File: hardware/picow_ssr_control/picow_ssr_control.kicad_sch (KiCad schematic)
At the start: 25 parts, among them Q1 IRF4905, U1 RaspberryPi-PicoW, U2 ULN2803A

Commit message: Added Copyright and logos etc.
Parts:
- S1: Mouser Part Number 774-1938MS -> (none)
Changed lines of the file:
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@@
   (title_block
     (title "Picow SSR Control")
-    (date "2022-07-23")
-    (rev "0.0.1")
+    (date "2022-07-26")
+    (rev "0.0.3")
     (comment 2 "http://creativecommons.org/licenses/by-sa/4.0/")
     (comment 3 "License: CC By SA 4.0")
@@
       (effects (font (size 1.27 1.27)) hide)
     )
-    (property "Mouser Part Number" "774-1938MS" (id 6) (at 238.76 135.89 0)
+    (property "Mouser Price/Stock" "https://www.mouser.com/ProductDetail/CTS-Electronic-Components/193-8MS?qs=Mr%252BgrRYddfpU71WCaMSCKA%3D%3D" (id 11) (at 241.3 135.89 0)
       (effects (font (size 1.27 1.27)) (justify left) hide)
     )
-    (property "Mouser Price/Stock" "https://www.mouser.com/ProductDetail/CTS-Electronic-Components/193-8MS?qs=Mr%252BgrRYddfpU71WCaMSCKA%3D%3D" (id 7) (at 241.3 135.89 0)
-      (effects (font (size 1.27 1.27)) (justify left) hide)
-    )

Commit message: Added Updated symbol, footprint, 3d model for zener diode
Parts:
- ZD1: footprint Diode_SMD:D_SMF -> Picow_control:BZD27C10P-M3-08; symbol Device:D_Zener_Small_Filled -> Picow_control:BZD27C10P-M3-08; Characteristics (none) -> 10V 800mW; Height (mm) (none) -> 1.08; MFN (none) -> Vishay Semiconductors; MFP (none) -> BZD27C10P-M3-08; Mfr Vishay Semiconductors -> (none); Mfr # BZD27C10P-M3-08 -> (none); Mouser # 78-BZD27C10P-M3-08 -> (none); Mouser Part Number (none) -> 78-BZD27C10P-M3-08; Mouser Price/Stock (none) -> https://www.mouser.com/ProductDetail/Vishay-Semiconductors/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; Package (none) -> SMF (DO-219AB); Type (none) -> SMD

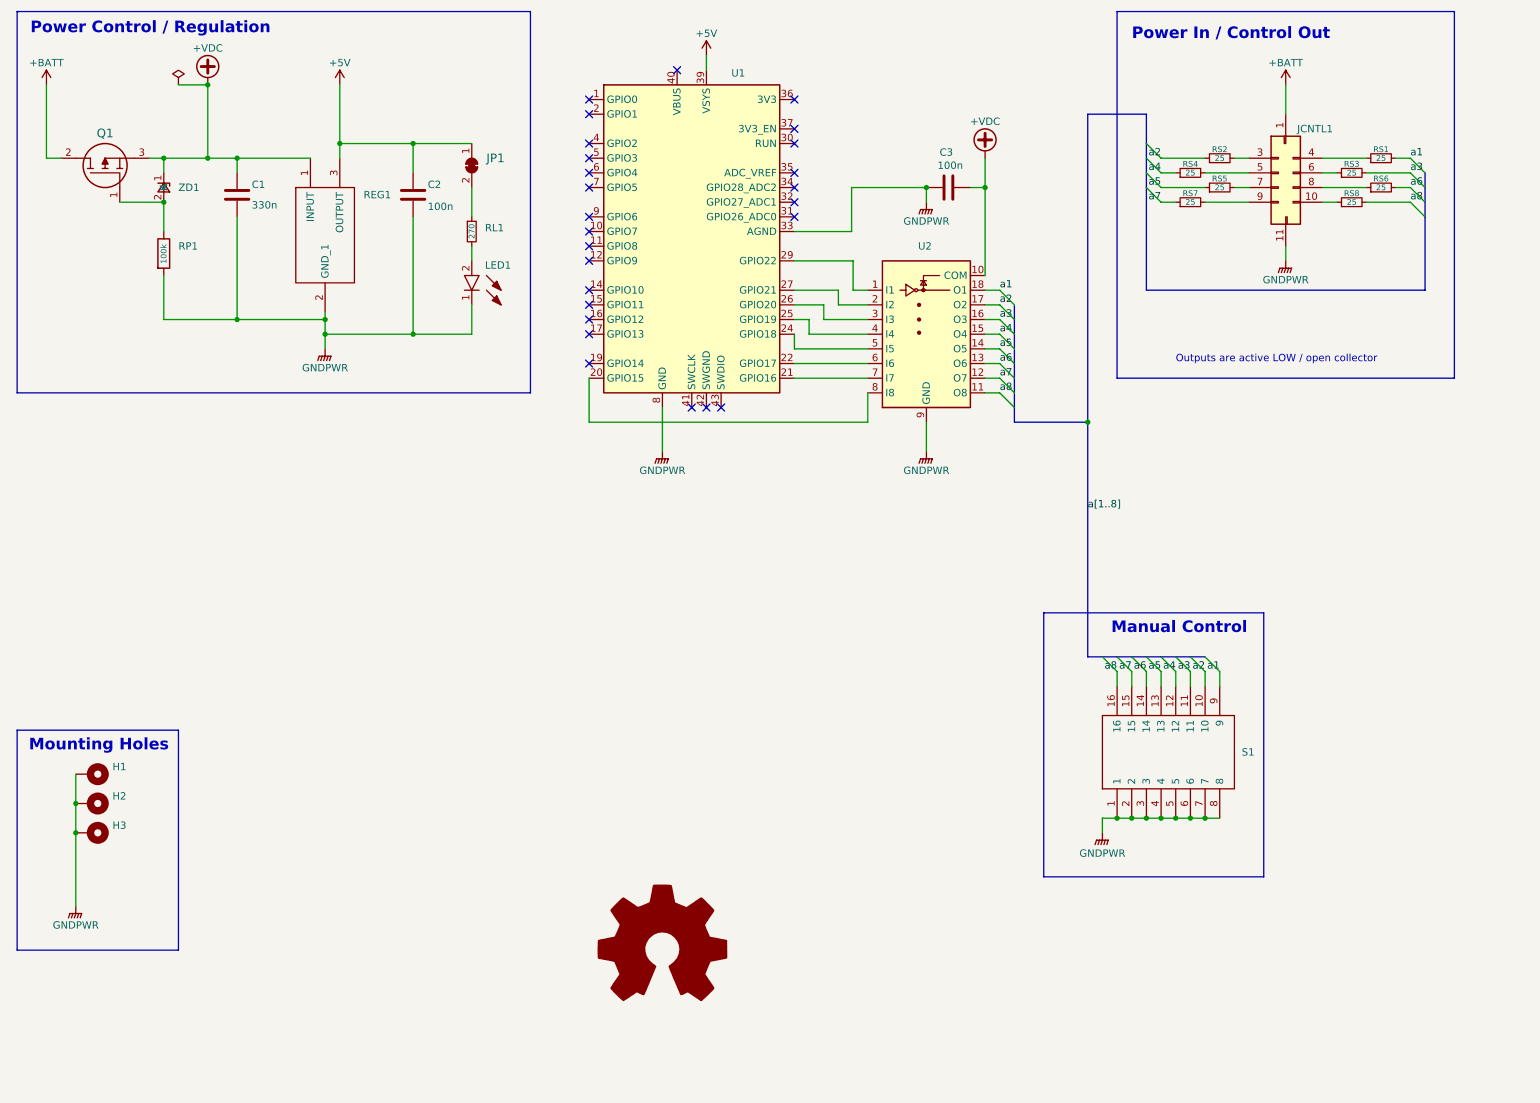
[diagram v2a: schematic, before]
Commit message: Add new Cern licensing info
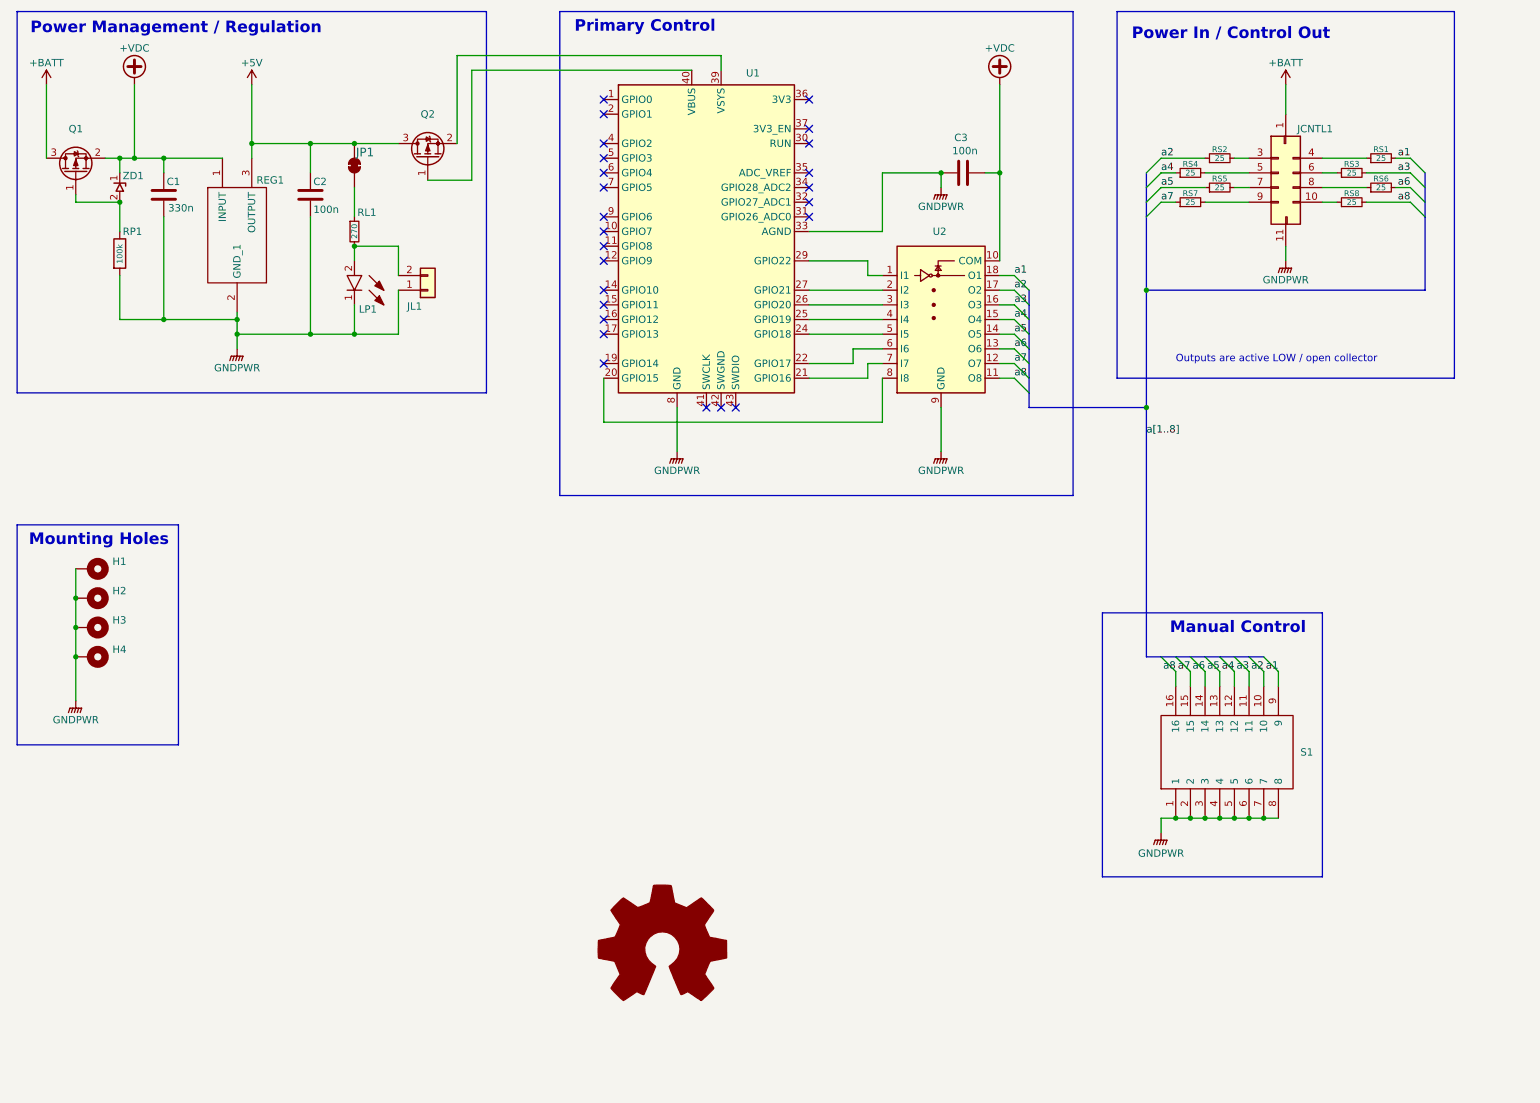
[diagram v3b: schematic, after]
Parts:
- removed Q1: IRF4905, dragon_mobile:TO254P469X1042X1967-3P, symbol dragon_mobile:IRF4905PBF
- added H4: MountingHole_Pad, MountingHole:MountingHole_3.2mm_M3_Pad_Via, symbol Mechanical:MountingHole_Pad
- added JL1: Conn_01x02, Connector_PinHeader_1.00mm:PinHeader_1x02_P1.00mm_Vertical, symbol Connector_Generic:Conn_01x02
- added Q1, Q2: DMG2301L, Package_TO_SOT_SMD:SOT-23, symbol Picow_control:DMG2301L
- RL1: Characteristics (none) -> 270Ohms; 300mW; SMD (0603) 5% Anti Surge AEC-Q200; MFN (none) -> ROHM Semiconductor; MFP (none) -> SDR03EZPJ271; Mfr. #: SDR03EZPJ271 -> (none); Mfr.: ROHM Semiconductor -> (none); Mouser #: 755-SDR03EZPJ271 -> (none); Mouser Part Number (none) -> 755-SDR03EZPJ271; Mouser Price/Stock (none) -> https://www.mouser.com/ProductDetail/ROHM-Semiconductor/SDR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; Package (none) -> 0603; Type (none) -> SMD
- RP1: Characteristics (none) -> 100Kohm 300mW 1% Anti Surge AEC-Q200; Height (mm) (none) -> 0.45; MFN (none) -> ROHM Semiconductor; MFP (none) -> SDR03EZPF1003; Mfr. #: SDR03EZPF1003 -> (none); Mfr.: ROHM Semiconductor -> (none); Mouser Part Number (none) -> 755-SDR03EZPF1003; Mouser Price/Stock (none) -> https://www.mouser.com/ProductDetail/ROHM-Semiconductor/SDR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; Package (none) -> 0603; Type (none) -> SMD
- renumbered LED1 to LP1
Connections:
- net +5V: now also Q2.3 (D); no longer U1.39 (VSYS)
- net +BATT: now also Q1.3 (D)
- net +VDC: now also Q1.2 (S)
- net GNDPWR: now also H4.1, JL1.1 (Pin_1)
- net at LP1.2, RL1.2: now also JL1.2 (Pin_2)
- net at U1.40 (VBUS): now also Q2.1 (G)
- net at RP1.1, ZD1.2: now also Q1.1 (G)
- new net: Q2.2 (S), U1.39 (VSYS)
- no-connect marks 26 -> 25
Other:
- note added: "Power Management / Regulation"
- note added: "Primary Control"
- note removed: "Power Control / Regulation"
- moved on the sheet: C1, C2, C3, H1, H2, H3, LP1, REG1, RL1, RP1, S1, U1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
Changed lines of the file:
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@@
     (title "Picow SSR Control")
     (date "2022-07-26")
-    (rev "0.0.3")
+    (rev "0.0.4")
     (comment 2 "http://creativecommons.org/licenses/by-sa/4.0/")
     (comment 3 "License: CC By SA 4.0")

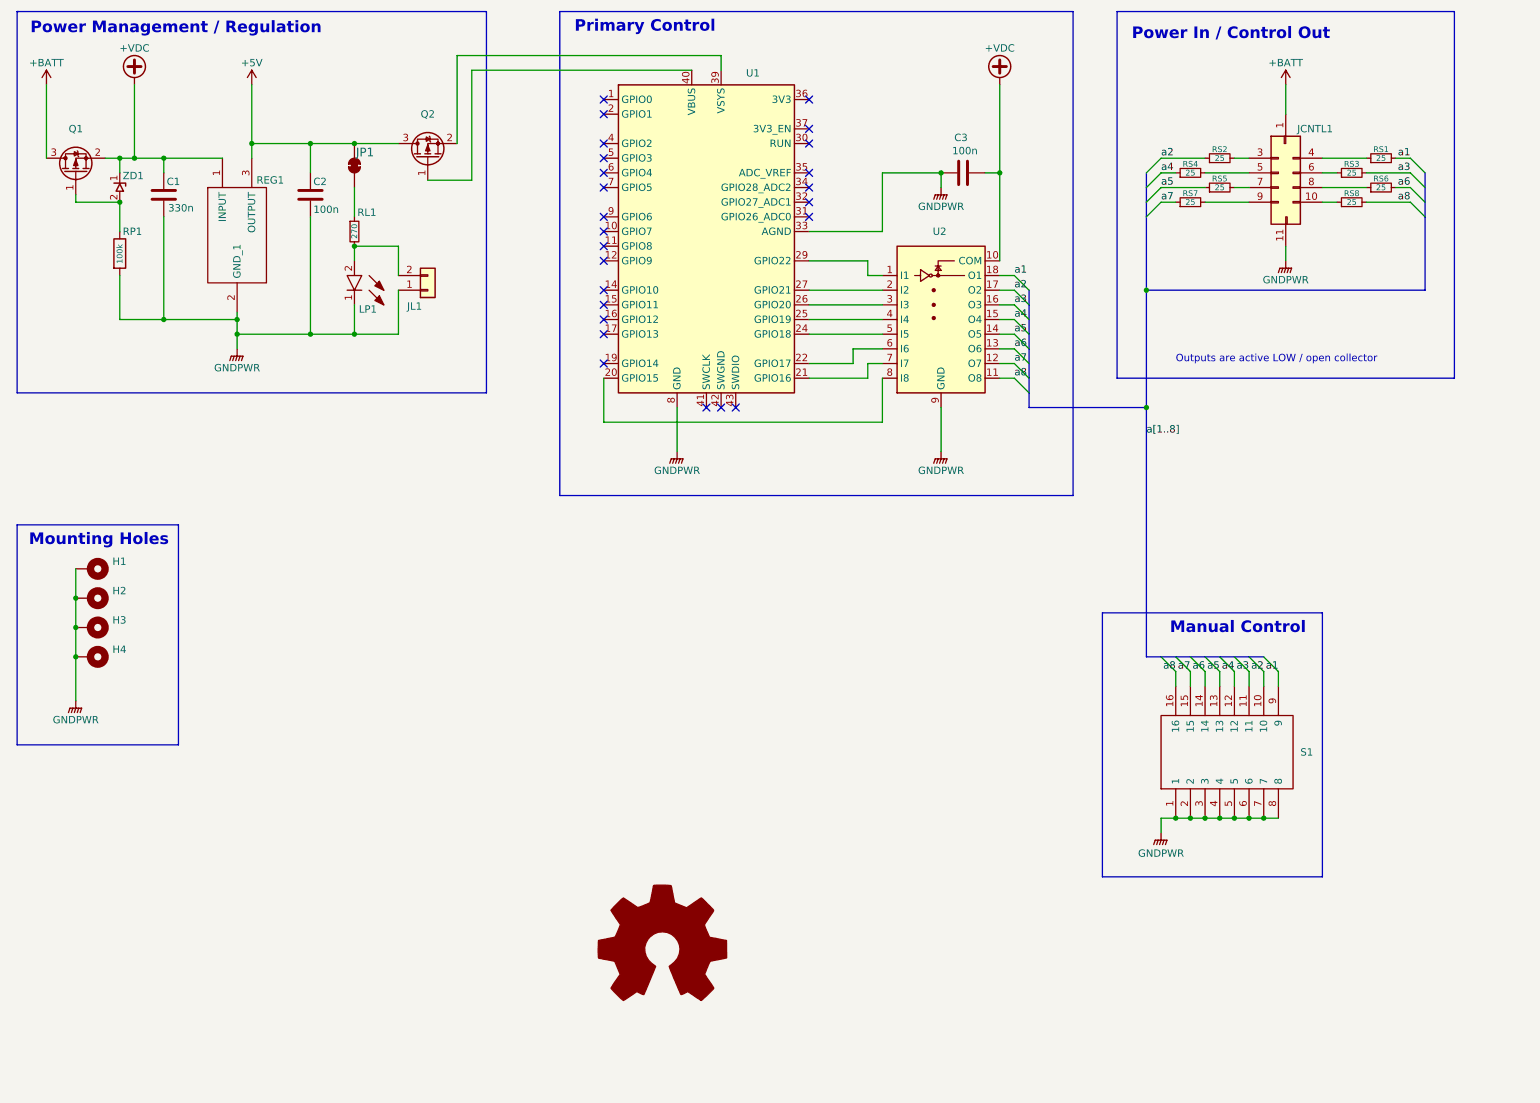
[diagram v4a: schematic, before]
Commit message: WIP control connector changes v0.0.7
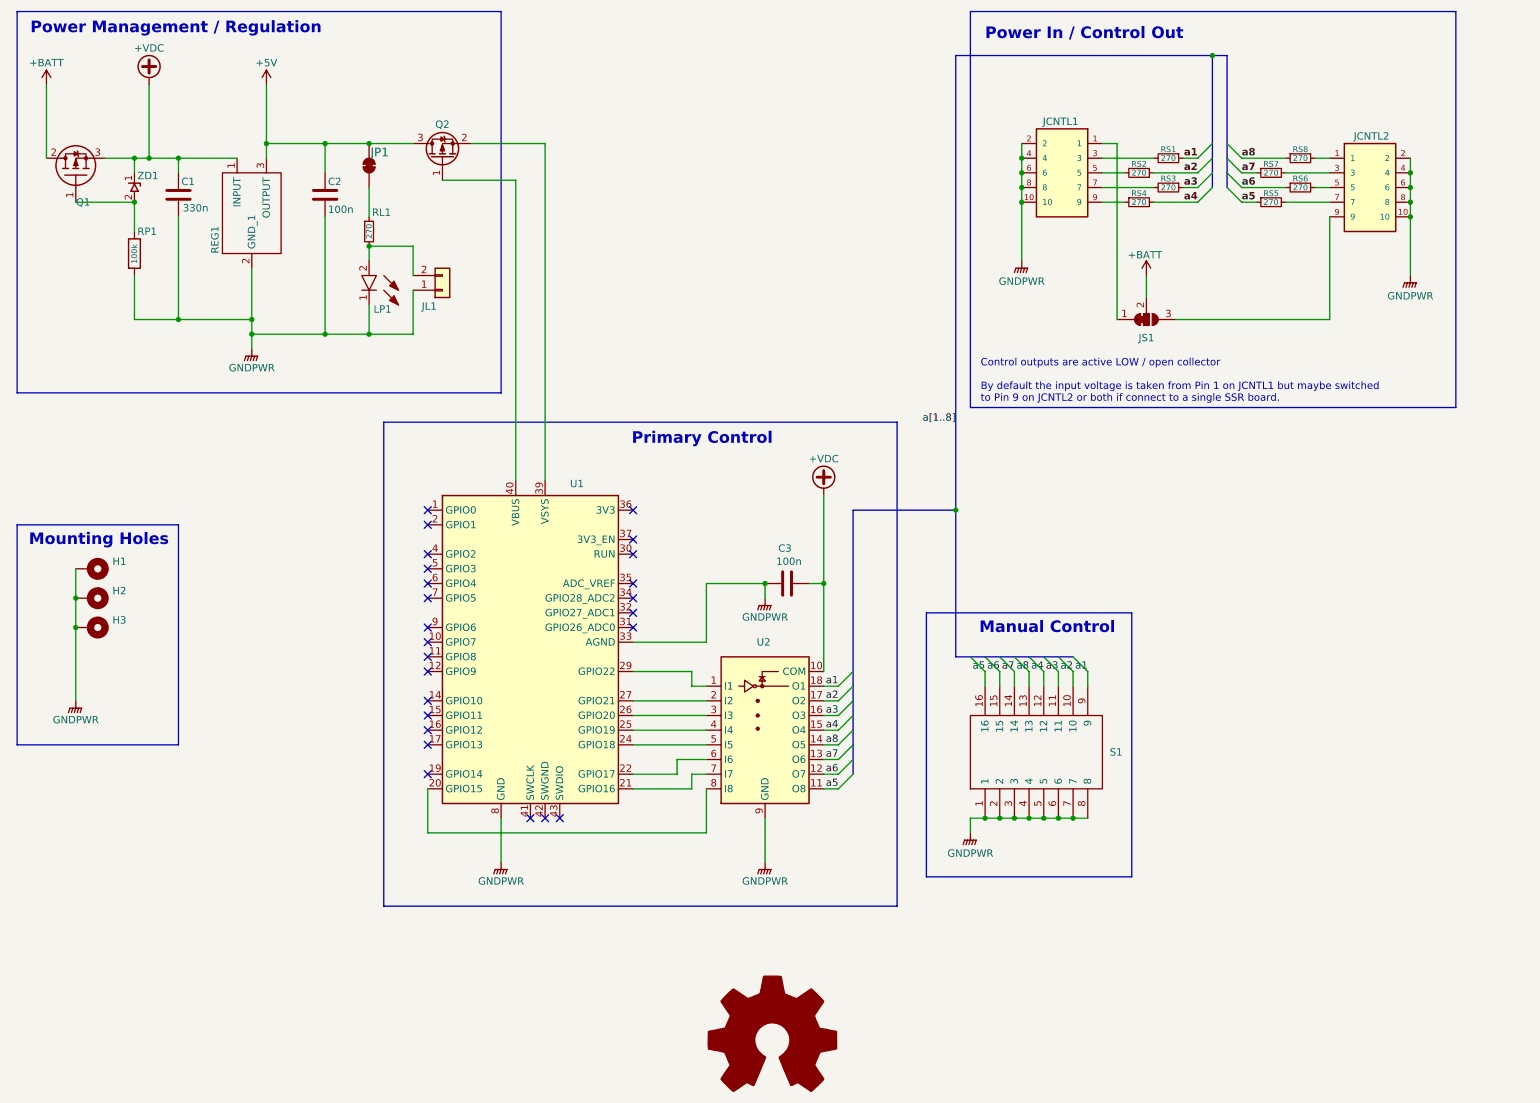
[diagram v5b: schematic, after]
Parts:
- removed H4: MountingHole_Pad, MountingHole:MountingHole_3.2mm_M3_Pad_Via, symbol Mechanical:MountingHole_Pad
- removed JCNTL1: Conn_02x06_Odd_Even, Connector_IDC:IDC-Header_2x06_P2.54mm_Horizontal, symbol Connector_Generic:Conn_02x06_Odd_Even
- removed Q1: DMG2301L, Package_TO_SOT_SMD:SOT-23, symbol Picow_control:DMG2301L
- added JCNTL1, JCNTL2: SHF-105-01-L-D-RA, dragon_mobile:SAMTEC_SHF-105-01-L-D-RA, symbol Connector_Samtec:SHF-105-01-L-D-RA
- added JS1: SolderJumper_3_Bridged12, Jumper:SolderJumper-3_P1.3mm_Bridged12_RoundedPad1.0x1.5mm_NumberLabels, symbol Jumper:SolderJumper_3_Bridged12
- added Q1: IRF4905PBF, dragon_mobile:TO254P469X1042X1967-3P, symbol dragon_mobile:IRF4905PBF
- LP1: Characteristics (none) -> Green LED (571 nm); Rectangle Lens; Top Viewing; 1608 (0603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; Height (mm) (none) -> 0.80; MFN (none) -> Lite-On; MFP (none) -> LTST-C190KGKT; Package (none) -> 0603; Type (none) -> SMD
- Q2: footprint Package_TO_SOT_SMD:SOT-23 -> Picow_control:DMG2301L
- REG1: footprint Package_TO_SOT_SMD:SOT-223 -> SOT230P700X180-4N
- RS1, RS2, RS3, RS4, RS5, RS6, RS7, RS8: value 25 -> 270; Characteristics (none) -> 270Ohms; 300mW; SMD (0603) 5% Anti Surge AEC-Q200; MFN (none) -> ROHM Semiconductor; MFP (none) -> SDR03EZPJ271; Mouser Part Number (none) -> 755-SDR03EZPJ271; Mouser Price/Stock (none) -> https://www.mouser.com/ProductDetail/ROHM-Semiconductor/SDR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; Package (none) -> 0603; Type (none) -> SMD
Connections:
- net +BATT: now also JS1.2 (C), Q1.2
- net +VDC: now also Q1.3
- net GNDPWR: now also JCNTL1.10, JCNTL1.2, JCNTL1.4, JCNTL1.6, JCNTL1.8, JCNTL2.10, JCNTL2.2, JCNTL2.4, JCNTL2.6, JCNTL2.8
- net a1: now also RS1.1; no longer RS1.2
- net a3: now also RS3.1; no longer RS3.2
- net a4: now also RS4.2; no longer RS4.1
- net a5: now also S1.16, U2.11 (O8); no longer S1.13, U2.14 (O5)
- net a6: now also RS6.1, S1.15, U2.12 (O7); no longer RS6.2, S1.14, U2.13 (O6)
- net a7: now also S1.14, U2.13 (O6); no longer S1.15, U2.12 (O7)
- net a8: now also RS8.1, S1.13, U2.14 (O5); no longer RS8.2, S1.16, U2.11 (O8)
- net at RS7.2: now also JCNTL2.3
- net at RP1.1, ZD1.2: now also Q1.1
- net at RS5.2: now also JCNTL2.7
- net at RS2.2: now also JCNTL1.5
- new net: JCNTL1.9, RS4.1
- new net: JCNTL1.1, JS1.1 (A)
- new net: JCNTL2.9, JS1.3 (B)
- new net: JCNTL2.1, RS8.2
- new net: JCNTL1.3, RS1.2
- new net: JCNTL1.7, RS3.2
- new net: JCNTL2.5, RS6.2
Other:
- note added: "Control outputs are active LOW / open collector By default the input voltage is taken from Pin 1 on JCNTL1 but maybe switched to Pin 9 on JCNTL2 or both if connect to a single SSR board."
- note removed: "Outputs are active LOW / open collector"
- moved on the sheet: C1, C2, C3, JL1, JP1, LP1, Q2, REG1, RL1, RP1, S1, U1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
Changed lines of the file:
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@@
   (title_block
     (title "Picow SSR Control")
-    (date "2022-08-05")
-    (rev "0.0.6")
+    (date "2022-12-07")
+    (rev "0.0.7")
     (comment 2 "http://creativecommons.org/licenses/by-sa/4.0/")
     (comment 3 "License: CC By SA 4.0")
